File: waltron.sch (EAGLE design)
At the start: 25 parts, among them IC1 4049N, U1 LM386

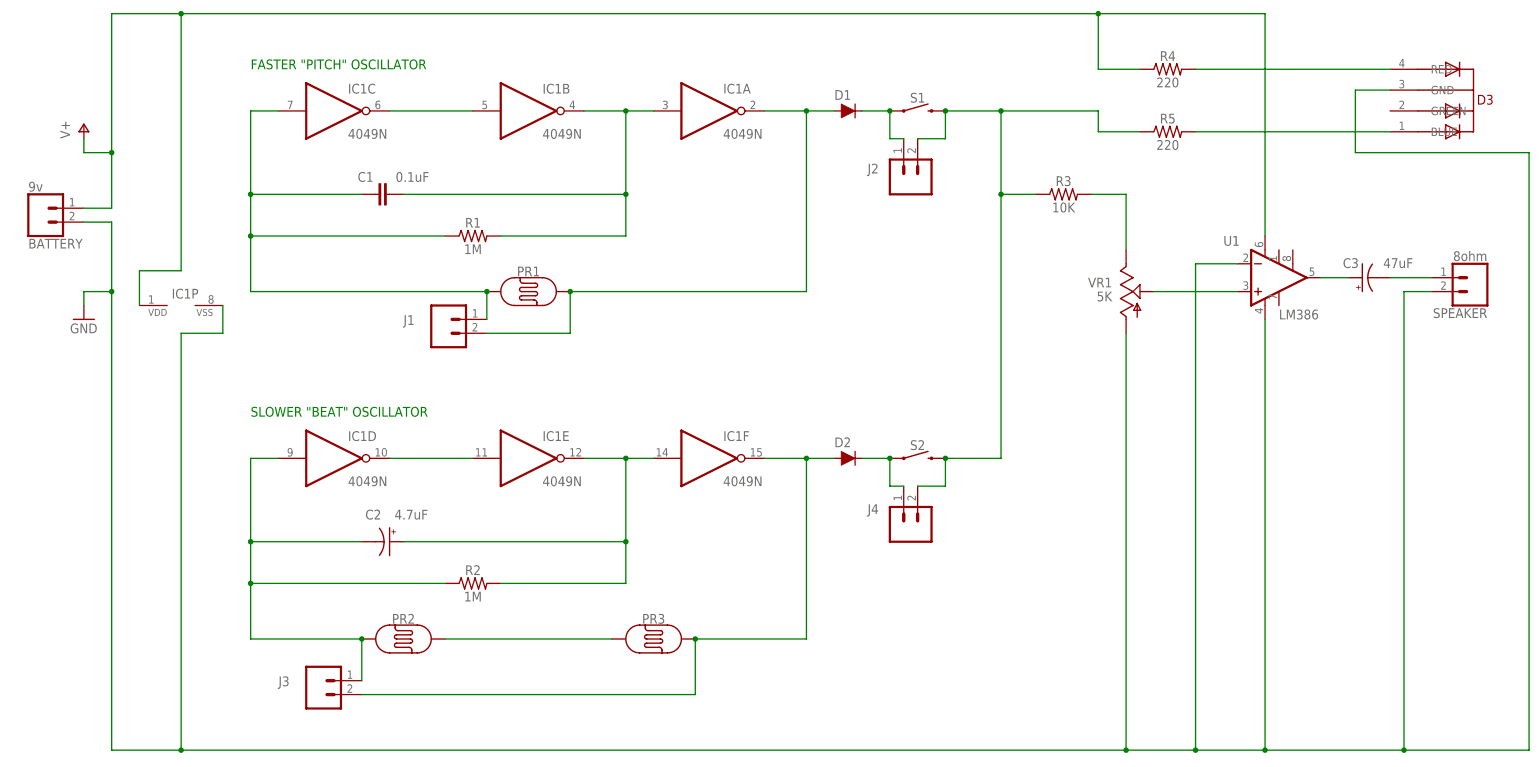
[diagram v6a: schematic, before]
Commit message: Optimize J connectors, reroute
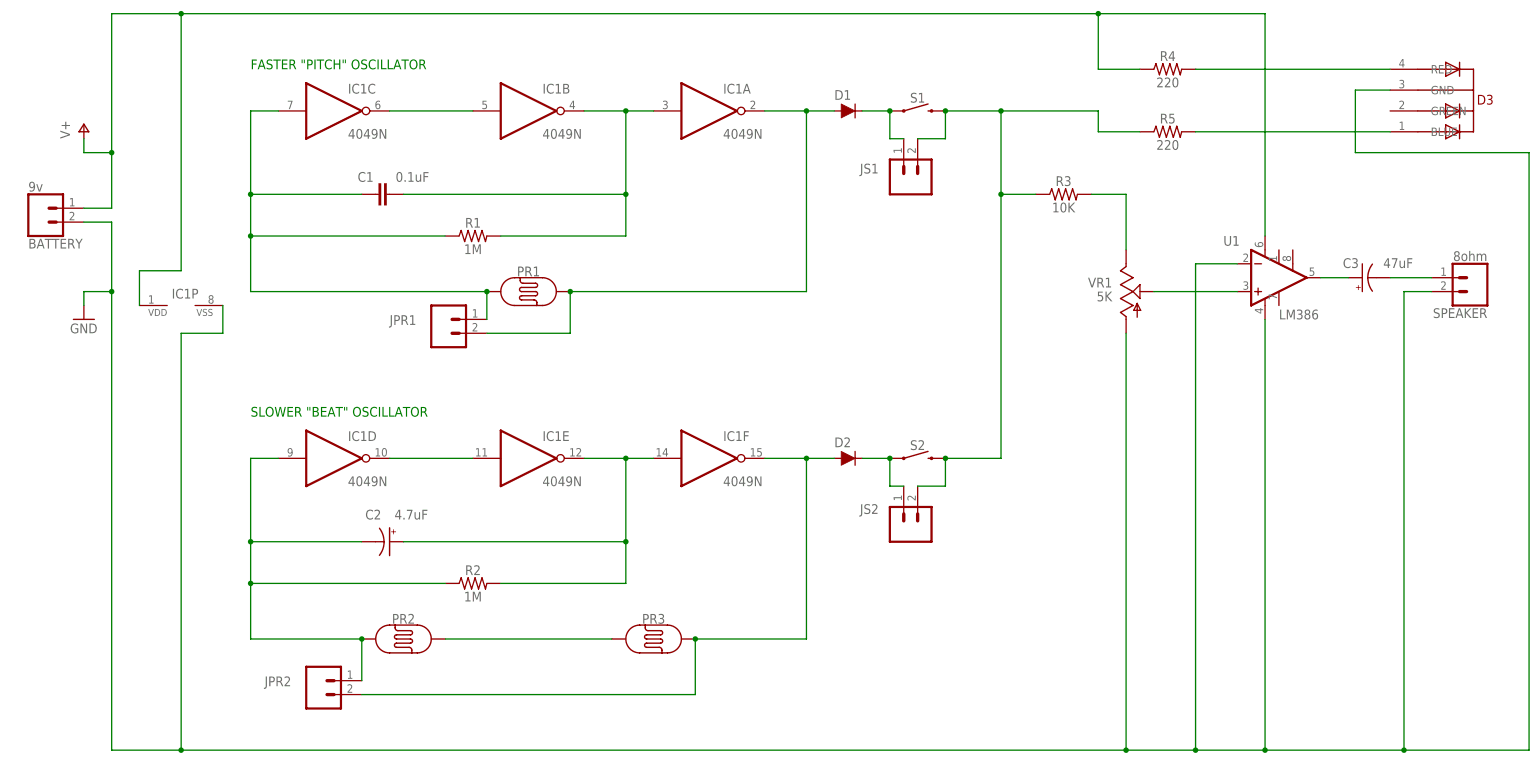
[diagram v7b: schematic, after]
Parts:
- renumbered J1 to JPR1, J2 to JS1, J3 to JPR2, J4 to JS2
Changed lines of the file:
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@@
 <setting verticaltext="up"/>
 </settings>
-<grid distance="0.000000123031" unitdist="inch" unit="inch" style="lines" multiple="1" display="no" altdistance="0.01" altunitdist="inch" altunit="inch"/>
+<grid distance="0.1" unitdist="inch" unit="inch" style="lines" multiple="1" display="no" altdistance="0.01" altunitdist="inch" altunit="inch"/>
 <layers>
 <layer number="1" name="Top" color="4" fill="1" visible="no" active="no"/>
@@
 <part name="GND1" library="supply1" deviceset="GND" device=""/>
 <part name="VR1" library="adafruit" deviceset="TRIM" device="" value="5K"/>
-<part name="J1" library="SparkFun-Connectors" deviceset="CONN_02" device=""/>
-<part name="J2" library="SparkFun-Connectors" deviceset="CONN_02" device=""/>
-<part name="J3" library="SparkFun-Connectors" deviceset="CONN_02" device=""/>
-<part name="J4" library="SparkFun-Connectors" deviceset="CONN_02" device=""/>
+<part name="JPR1" library="SparkFun-Connectors" deviceset="CONN_02" device=""/>
+<part name="JS1" library="SparkFun-Connectors" deviceset="CONN_02" device=""/>
+<part name="JPR2" library="SparkFun-Connectors" deviceset="CONN_02" device=""/>
+<part name="JS2" library="SparkFun-Connectors" deviceset="CONN_02" device=""/>
 <part name="D3" library="adafruit" deviceset="5MMRGBLED" device=""/>
 </parts>
@@
 <attribute name="VALUE" x="142.24" y="35.56" size="1.778" layer="96" rot="R180"/>
 </instance>
-<instance part="J1" gate="G$1" x="20.32" y="30.48" smashed="yes" rot="MR180">
+<instance part="JPR1" gate="G$1" x="20.32" y="30.48" smashed="yes" rot="MR180">
 <attribute name="VALUE" x="17.78" y="35.306" size="1.778" layer="96" font="vector" rot="MR180"/>
-<attribute name="NAME" x="12.7" y="31.242" size="1.778" layer="95" font="vector" rot="MR180"/>
-</instance>
-<instance part="J2" gate="G$1" x="104.14" y="55.88" smashed="yes" rot="MR90">
+<attribute name="NAME" x="10.16" y="31.242" size="1.778" layer="95" font="vector" rot="MR180"/>
+</instance>
+<instance part="JS1" gate="G$1" x="104.14" y="55.88" smashed="yes" rot="MR90">
 <attribute name="VALUE" x="99.314" y="53.34" size="1.778" layer="96" font="vector" rot="MR90"/>
 <attribute name="NAME" x="99.568" y="57.15" size="1.778" layer="95" font="vector" rot="MR0"/>
 </instance>
-<instance part="J3" gate="G$1" x="-2.54" y="-35.56" smashed="yes" rot="MR180">
+<instance part="JPR2" gate="G$1" x="-2.54" y="-35.56" smashed="yes" rot="MR180">
 <attribute name="VALUE" x="-5.08" y="-30.734" size="1.778" layer="96" font="vector" rot="MR180"/>
-<attribute name="NAME" x="-10.16" y="-34.798" size="1.778" layer="95" font="vector" rot="MR180"/>
-</instance>
-<instance part="J4" gate="G$1" x="104.14" y="-7.62" smashed="yes" rot="MR90">
+<attribute name="NAME" x="-12.7" y="-34.798" size="1.778" layer="95" font="vector" rot="MR180"/>
+</instance>
+<instance part="JS2" gate="G$1" x="104.14" y="-7.62" smashed="yes" rot="MR90">
 <attribute name="VALUE" x="99.314" y="-10.16" size="1.778" layer="96" font="vector" rot="MR90"/>
 <attribute name="NAME" x="99.568" y="-5.08" size="1.778" layer="95" font="vector" rot="MR0"/>
@@
 <wire x1="5.08" y1="53.34" x2="-15.24" y2="53.34" width="0.1524" layer="91"/>
 <junction x="-15.24" y="53.34"/>
-<pinref part="J1" gate="G$1" pin="1"/>
+<pinref part="JPR1" gate="G$1" pin="1"/>
 <wire x1="27.94" y1="30.48" x2="27.94" y2="35.56" width="0.1524" layer="91"/>
 <junction x="27.94" y="35.56"/>
@@
 <wire x1="86.36" y1="68.58" x2="91.44" y2="68.58" width="0.1524" layer="91"/>
 <junction x="86.36" y="68.58"/>
-<pinref part="J1" gate="G$1" pin="2"/>
+<pinref part="JPR1" gate="G$1" pin="2"/>
 <wire x1="27.94" y1="27.94" x2="43.18" y2="27.94" width="0.1524" layer="91"/>
 <wire x1="43.18" y1="27.94" x2="43.18" y2="35.56" width="0.1524" layer="91"/>
@@
 <pinref part="PR2" gate="G$1" pin="P$1"/>
 <wire x1="-15.24" y1="-27.94" x2="5.08" y2="-27.94" width="0.1524" layer="91"/>
-<pinref part="J3" gate="G$1" pin="1"/>
+<pinref part="JPR2" gate="G$1" pin="1"/>
 <wire x1="5.08" y1="-35.56" x2="5.08" y2="-27.94" width="0.1524" layer="91"/>
 <junction x="5.08" y="-27.94"/>
@@
 <wire x1="66.04" y1="-27.94" x2="66.04" y2="-38.1" width="0.1524" layer="91"/>
 <junction x="66.04" y="-27.94"/>
-<pinref part="J3" gate="G$1" pin="2"/>
+<pinref part="JPR2" gate="G$1" pin="2"/>
 <wire x1="66.04" y1="-38.1" x2="5.08" y2="-38.1" width="0.1524" layer="91"/>
 </segment>
@@
 <pinref part="R5" gate="G$1" pin="1"/>
 <wire x1="139.7" y1="64.77" x2="147.32" y2="64.77" width="0.1524" layer="91"/>
-<pinref part="J2" gate="G$1" pin="2"/>
+<pinref part="JS1" gate="G$1" pin="2"/>
 <wire x1="106.68" y1="63.5" x2="111.76" y2="63.5" width="0.1524" layer="91"/>
 <wire x1="111.76" y1="63.5" x2="111.76" y2="68.58" width="0.1524" layer="91"/>
 <junction x="111.76" y="68.58"/>
-<pinref part="J4" gate="G$1" pin="2"/>
+<pinref part="JS2" gate="G$1" pin="2"/>
 <wire x1="106.68" y1="0" x2="111.76" y2="0" width="0.1524" layer="91"/>
 <wire x1="111.76" y1="0" x2="111.76" y2="5.08" width="0.1524" layer="91"/>
@@
 <wire x1="101.6" y1="68.58" x2="101.6" y2="63.5" width="0.1524" layer="91"/>
 <junction x="101.6" y="68.58"/>
-<pinref part="J2" gate="G$1" pin="1"/>
+<pinref part="JS1" gate="G$1" pin="1"/>
 <wire x1="101.6" y1="63.5" x2="104.14" y2="63.5" width="0.1524" layer="91"/>
 </segment>
@@
 <wire x1="101.6" y1="5.08" x2="101.6" y2="0" width="0.1524" layer="91"/>
 <junction x="101.6" y="5.08"/>
-<pinref part="J4" gate="G$1" pin="1"/>
+<pinref part="JS2" gate="G$1" pin="1"/>
 <wire x1="101.6" y1="0" x2="104.14" y2="0" width="0.1524" layer="91"/>
 </segment>

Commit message: Update schematic w/ 2999.1 concerns
- use IC name for LM386 instead of U1
- switch trim pot to model used in 4step
- add switch connection
- consistent J names for speaker and battery
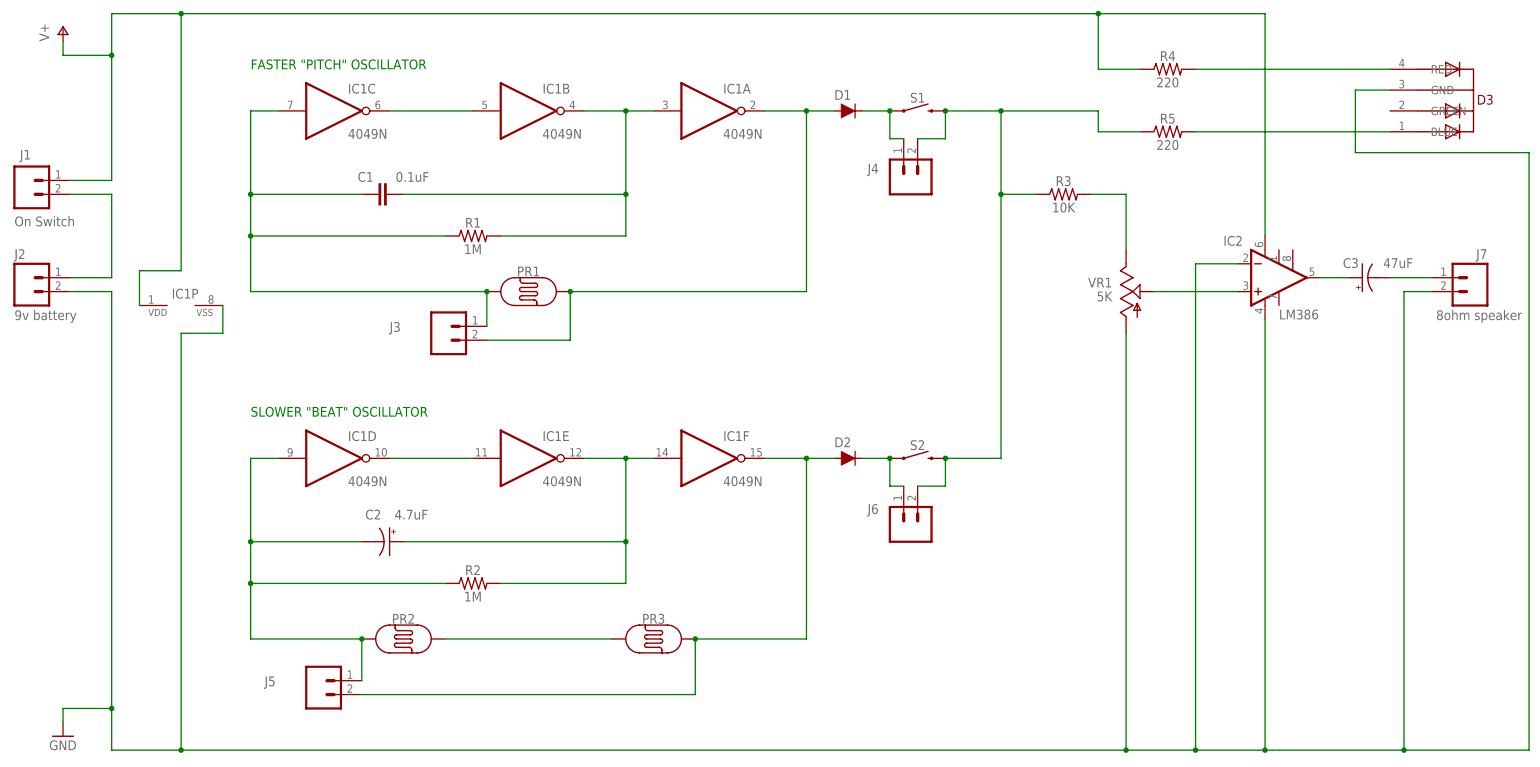
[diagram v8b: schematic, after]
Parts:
- removed BATTERY: 9v, SparkFun-Connectors:CONN_02
- removed JPR1: (no value), SparkFun-Connectors:CONN_02
- added J1: On Switch, SparkFun-Connectors:CONN_02
- added J2: 9v battery, SparkFun-Connectors:CONN_02
- added J3: (no value), SparkFun-Connectors:CONN_02
- J7: value 8ohm -> 8ohm speaker
- renumbered JPR2 to J5, JS1 to J4, JS2 to J6, SPEAKER to J7, U1 to IC2
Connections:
- new net N$19: J1.2, J2.1
- net GND: now also J2.2; no longer BATTERY.2
- net N$3: now also J3.1; no longer JPR1.1
- net N$4: now also J3.2; no longer JPR1.2
- net V+: now also J1.1; no longer BATTERY.1
